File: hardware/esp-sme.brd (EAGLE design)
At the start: 58.4 x 35.6 mm, 37 parts, among them J2 BME280, J3 UART, Q3 NPN, Q4 NPN, Q5 NPN, U2 MIC5504

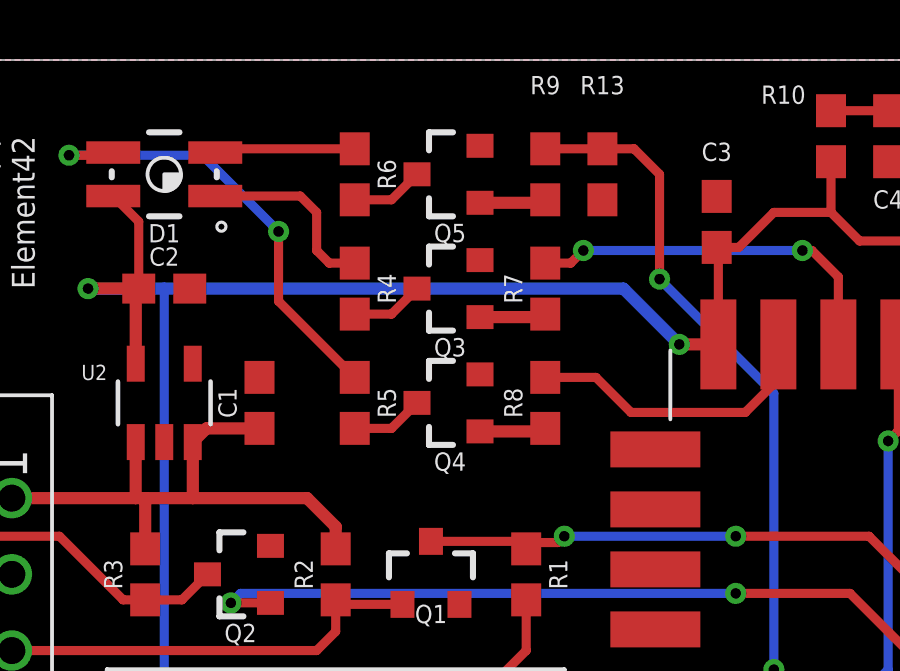
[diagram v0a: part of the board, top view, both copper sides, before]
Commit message: Replaced transistor for n-channel mosfet
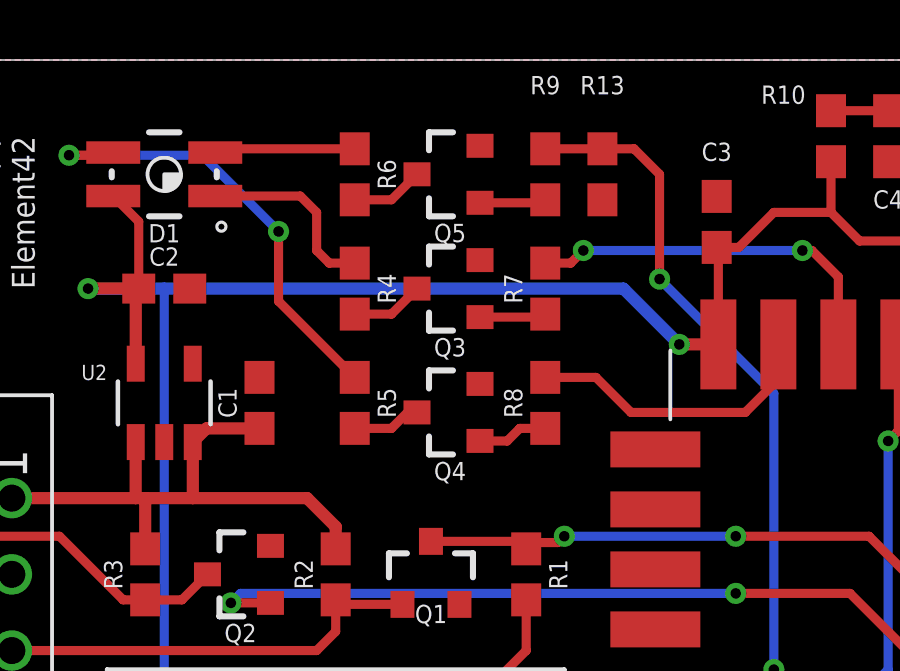
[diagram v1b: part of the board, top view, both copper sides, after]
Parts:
- Q3, Q4, Q5: value NPN -> (none)
- moved Q4 0.32 mm to (26.0, 22.5)
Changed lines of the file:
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@@
 <attribute name="PROD_ID" value="TRANS-12988" x="19.05" y="17.145" size="1.778" layer="27" rot="R90" display="off"/>
-</element>
-<element name="Q3" library="SparkFun-DiscreteSemi" library_urn="urn:adsk.eagle:library:514" package="SOT23-3" package3d_urn="urn:adsk.eagle:package:38446/1" value="NPN" x="26.035" y="26.67" smashed="yes" rot="R90">
-<attribute name="NAME" x="26.035" y="25.019" size="0.6096" layer="25" font="vector" ratio="20" rot="R180" align="bottom-center"/>
-<attribute name="PROD_ID" value="TRANS-08049" x="26.035" y="26.67" size="1.778" layer="27" rot="R90" display="off"/>
-</element>
-<element name="Q4" library="SparkFun-DiscreteSemi" library_urn="urn:adsk.eagle:library:514" package="SOT23-3" package3d_urn="urn:adsk.eagle:package:38446/1" value="NPN" x="26.035" y="22.86" smashed="yes" rot="R90">
-<attribute name="NAME" x="26.035" y="21.209" size="0.6096" layer="25" font="vector" ratio="20" rot="R180" align="bottom-center"/>
-<attribute name="PROD_ID" value="TRANS-08049" x="26.035" y="22.86" size="1.778" layer="27" rot="R90" display="off"/>
-</element>
-<element name="Q5" library="SparkFun-DiscreteSemi" library_urn="urn:adsk.eagle:library:514" package="SOT23-3" package3d_urn="urn:adsk.eagle:package:38446/1" value="NPN" x="26.035" y="30.48" smashed="yes" rot="R90">
-<attribute name="NAME" x="26.035" y="28.829" size="0.6096" layer="25" font="vector" ratio="20" rot="R180" align="bottom-center"/>
-<attribute name="PROD_ID" value="TRANS-08049" x="26.035" y="30.48" size="1.778" layer="27" rot="R90" display="off"/>
 </element>
 <element name="R1" library="SparkFun-Resistors" library_urn="urn:adsk.eagle:library:532" package="0603" package3d_urn="urn:adsk.eagle:package:39650/1" value="10k" x="28.575" y="17.145" rot="R270">
@@
 <element name="R15" library="SparkFun-Resistors" library_urn="urn:adsk.eagle:library:532" package="0603" package3d_urn="urn:adsk.eagle:package:39650/1" value="10k" x="20.955" y="9.525" rot="MR90">
 <attribute name="PROD_ID" value="RES-00824" x="20.955" y="9.525" size="1.778" layer="28" rot="MR90" display="off"/>
+</element>
+<element name="Q3" library="SparkFun-DiscreteSemi" library_urn="urn:adsk.eagle:library:514" package="SOT23-3" package3d_urn="urn:adsk.eagle:package:38446/1" value="" x="26.035" y="26.67" rot="R90">
+<attribute name="PROD_ID" value="TRANS-12988" x="26.035" y="26.67" size="1.778" layer="27" rot="R90" display="off"/>
+</element>
+<element name="Q4" library="SparkFun-DiscreteSemi" library_urn="urn:adsk.eagle:library:514" package="SOT23-3" package3d_urn="urn:adsk.eagle:package:38446/1" value="" x="26.035" y="22.5425" rot="R90">
+<attribute name="PROD_ID" value="TRANS-12988" x="26.035" y="22.5425" size="1.778" layer="27" rot="R90" display="off"/>
+</element>
+<element name="Q5" library="SparkFun-DiscreteSemi" library_urn="urn:adsk.eagle:library:514" package="SOT23-3" package3d_urn="urn:adsk.eagle:package:38446/1" value="" x="26.035" y="30.48" rot="R90">
+<attribute name="PROD_ID" value="TRANS-12988" x="26.035" y="30.48" size="1.778" layer="27" rot="R90" display="off"/>
 </element>
 </elements>
@@
 <contactref element="C3" pad="2"/>
 <contactref element="Q1" pad="2"/>
-<contactref element="Q3" pad="2"/>
 <contactref element="Q2" pad="2"/>
 <contactref element="J2" pad="2"/>
@@
 <contactref element="C5" pad="2"/>
 <contactref element="R13" pad="1"/>
-<contactref element="Q4" pad="2"/>
-<contactref element="Q5" pad="2"/>
 <polygon width="0.1524" layer="16">
 <vertex x="0" y="34.29"/>
@@
 <vertex x="0" y="-1.27"/>
 </polygon>
+<contactref element="Q3" pad="2"/>
+<contactref element="Q4" pad="2"/>
+<contactref element="Q5" pad="2"/>
 </signal>
 <signal name="P1_CTS">
@@
 <wire x1="32.17" y1="31.33" x2="31.115" y2="31.33" width="0.3048" layer="1"/>
 </signal>
-<signal name="N$4">
-<contactref element="R6" pad="2"/>
-<contactref element="Q5" pad="3"/>
-<wire x1="24.935" y1="30.48" x2="24.085" y2="29.63" width="0.3048" layer="1"/>
-<wire x1="24.085" y1="29.63" x2="22.86" y2="29.63" width="0.3048" layer="1"/>
-</signal>
 <signal name="N$5">
 <contactref element="R5" pad="2"/>
+<wire x1="22.86" y1="22.01" x2="24.085" y2="22.01" width="0.3048" layer="1"/>
 <contactref element="Q4" pad="3"/>
-<wire x1="24.935" y1="22.86" x2="24.085" y2="22.01" width="0.3048" layer="1"/>
-<wire x1="24.085" y1="22.01" x2="22.86" y2="22.01" width="0.3048" layer="1"/>
+<wire x1="24.085" y1="22.01" x2="24.6175" y2="22.5425" width="0.3048" layer="1"/>
+<wire x1="24.6175" y1="22.5425" x2="24.935" y2="22.5425" width="0.3048" layer="1"/>
 </signal>
 <signal name="N$6">
+<contactref element="R4" pad="2"/>
+<wire x1="22.86" y1="25.82" x2="24.085" y2="25.82" width="0.3048" layer="1"/>
 <contactref element="Q3" pad="3"/>
-<contactref element="R4" pad="2"/>
-<wire x1="24.935" y1="26.67" x2="24.085" y2="25.82" width="0.3048" layer="1"/>
-<wire x1="24.085" y1="25.82" x2="22.86" y2="25.82" width="0.3048" layer="1"/>
+<wire x1="24.085" y1="25.82" x2="24.935" y2="26.67" width="0.3048" layer="1"/>
 </signal>
 <signal name="N$1">
@@
 </signal>
 <signal name="N$7">
+<contactref element="R9" pad="1"/>
+<wire x1="29.11" y1="29.53" x2="29.21" y2="29.63" width="0.4064" layer="1"/>
 <contactref element="Q5" pad="1"/>
-<contactref element="R9" pad="1"/>
-<wire x1="27.035" y1="29.53" x2="29.11" y2="29.53" width="0.4064" layer="1"/>
-<wire x1="29.11" y1="29.53" x2="29.21" y2="29.63" width="0.4064" layer="1"/>
+<wire x1="27.035" y1="29.53" x2="29.11" y2="29.53" width="0.3048" layer="1"/>
 </signal>
 <signal name="N$8">
+<contactref element="R8" pad="1"/>
+<wire x1="29.11" y1="21.91" x2="29.21" y2="22.01" width="0.4064" layer="1"/>
 <contactref element="Q4" pad="1"/>
-<contactref element="R8" pad="1"/>
-<wire x1="27.035" y1="21.91" x2="29.11" y2="21.91" width="0.4064" layer="1"/>
-<wire x1="29.11" y1="21.91" x2="29.21" y2="22.01" width="0.4064" layer="1"/>
+<wire x1="29.21" y1="22.01" x2="28.36" y2="22.01" width="0.3048" layer="1"/>
+<wire x1="28.36" y1="22.01" x2="27.94" y2="21.59" width="0.3048" layer="1"/>
+<wire x1="27.94" y1="21.59" x2="27.0375" y2="21.59" width="0.3048" layer="1"/>
+<wire x1="27.0375" y1="21.59" x2="27.035" y2="21.5925" width="0.3048" layer="1"/>
 </signal>
 <signal name="N$9">
+<contactref element="R7" pad="1"/>
+<wire x1="29.11" y1="25.72" x2="29.21" y2="25.82" width="0.4064" layer="1"/>
 <contactref element="Q3" pad="1"/>
-<contactref element="R7" pad="1"/>
-<wire x1="27.035" y1="25.72" x2="29.11" y2="25.72" width="0.4064" layer="1"/>
-<wire x1="29.11" y1="25.72" x2="29.21" y2="25.82" width="0.4064" layer="1"/>
+<wire x1="27.035" y1="25.72" x2="29.11" y2="25.72" width="0.3048" layer="1"/>
 </signal>
 <signal name="N$11">
@@
 <wire x1="40.98" y1="6.3725" x2="39.515" y2="4.9075" width="0.3048" layer="1"/>
 </signal>
+<signal name="N$4">
+<contactref element="R6" pad="2"/>
+<contactref element="Q5" pad="3"/>
+<wire x1="22.86" y1="29.63" x2="24.085" y2="29.63" width="0.3048" layer="1"/>
+<wire x1="24.085" y1="29.63" x2="24.935" y2="30.48" width="0.3048" layer="1"/>
+</signal>
 </signals>
